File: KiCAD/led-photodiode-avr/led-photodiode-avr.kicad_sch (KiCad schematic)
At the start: 40 parts, among them J1 Screw_Terminal_01x02, J2 Conn_02x08_Odd_Even, J3 ISP, J4 Conn_01x06_Pin, U1 REF3040, U2 L78L05_SOT89, U3 OPA350, U4 L78L05_SOT89, U5 DDC112, U7 ATmega328-A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

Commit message: working on BOM
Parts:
- C1: value 0.47uF -> 0.33uF; DigikeyNumber (none) -> 1276-1123-1-ND; ManufacturerNumber (none) -> CL21B334KBFNNNE
- C10, C12, C14, C23, C3, C5, C54, C55, C6, C8: DigikeyNumber (none) -> 478-KGM21NR71H104KTCT-ND; ManufacturerNumber (none) -> KGM21NR71H104KT
- C11, C13, C4, C9: DigikeyNumber (none) -> 1292-0805X106K250CT-ND; ManufacturerNumber (none) -> 0805X106K250CT
- C19, C20: now not fitted
- C2, C7: DigikeyNumber (none) -> 1276-1123-1-ND; ManufacturerNumber (none) -> CL21B334KBFNNNE
- C52: DigikeyNumber (none) -> 1276-1029-1-ND; ManufacturerNumber (none) -> CL21B105KBFNNNE
- D3: DigikeyNumber (none) -> 1516-QBLP631-R3ACT-ND; ManufacturerNumber (none) -> QBLP631-R3A
- J1: DigikeyNumber (none) -> A98076-ND; ManufacturerNumber (none) -> 282836-2

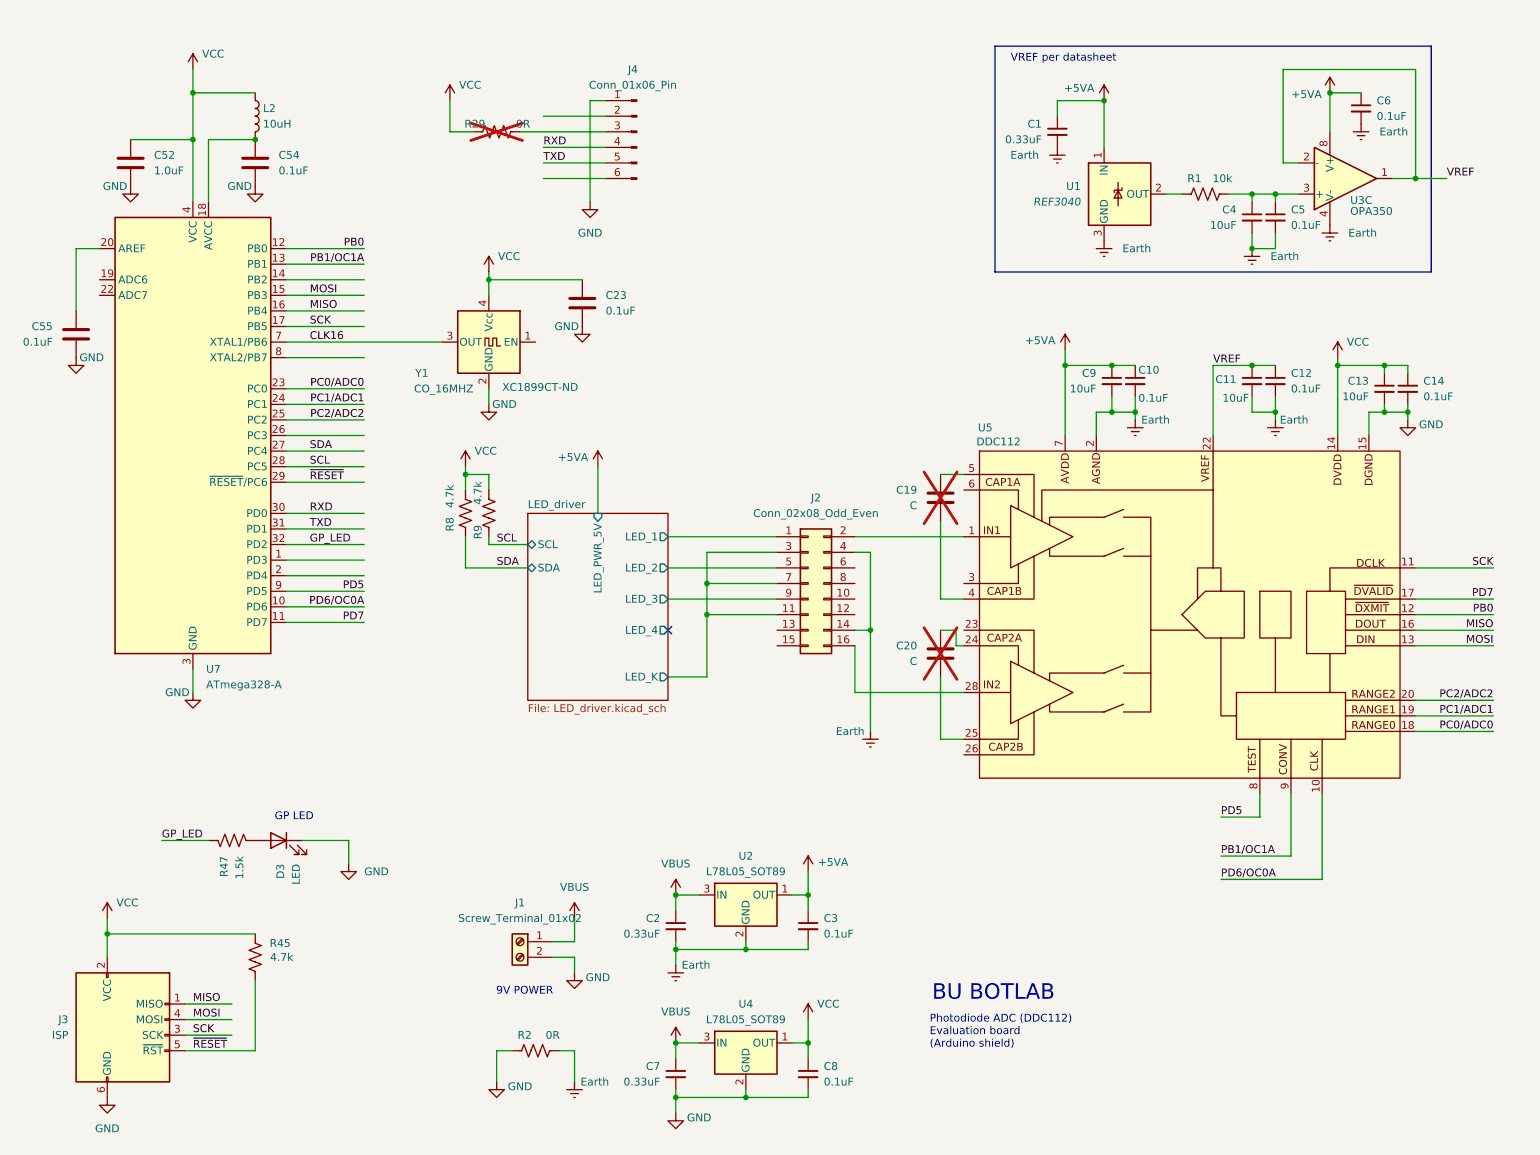
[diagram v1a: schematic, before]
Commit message: many schematic tweaks; add fields for BOM
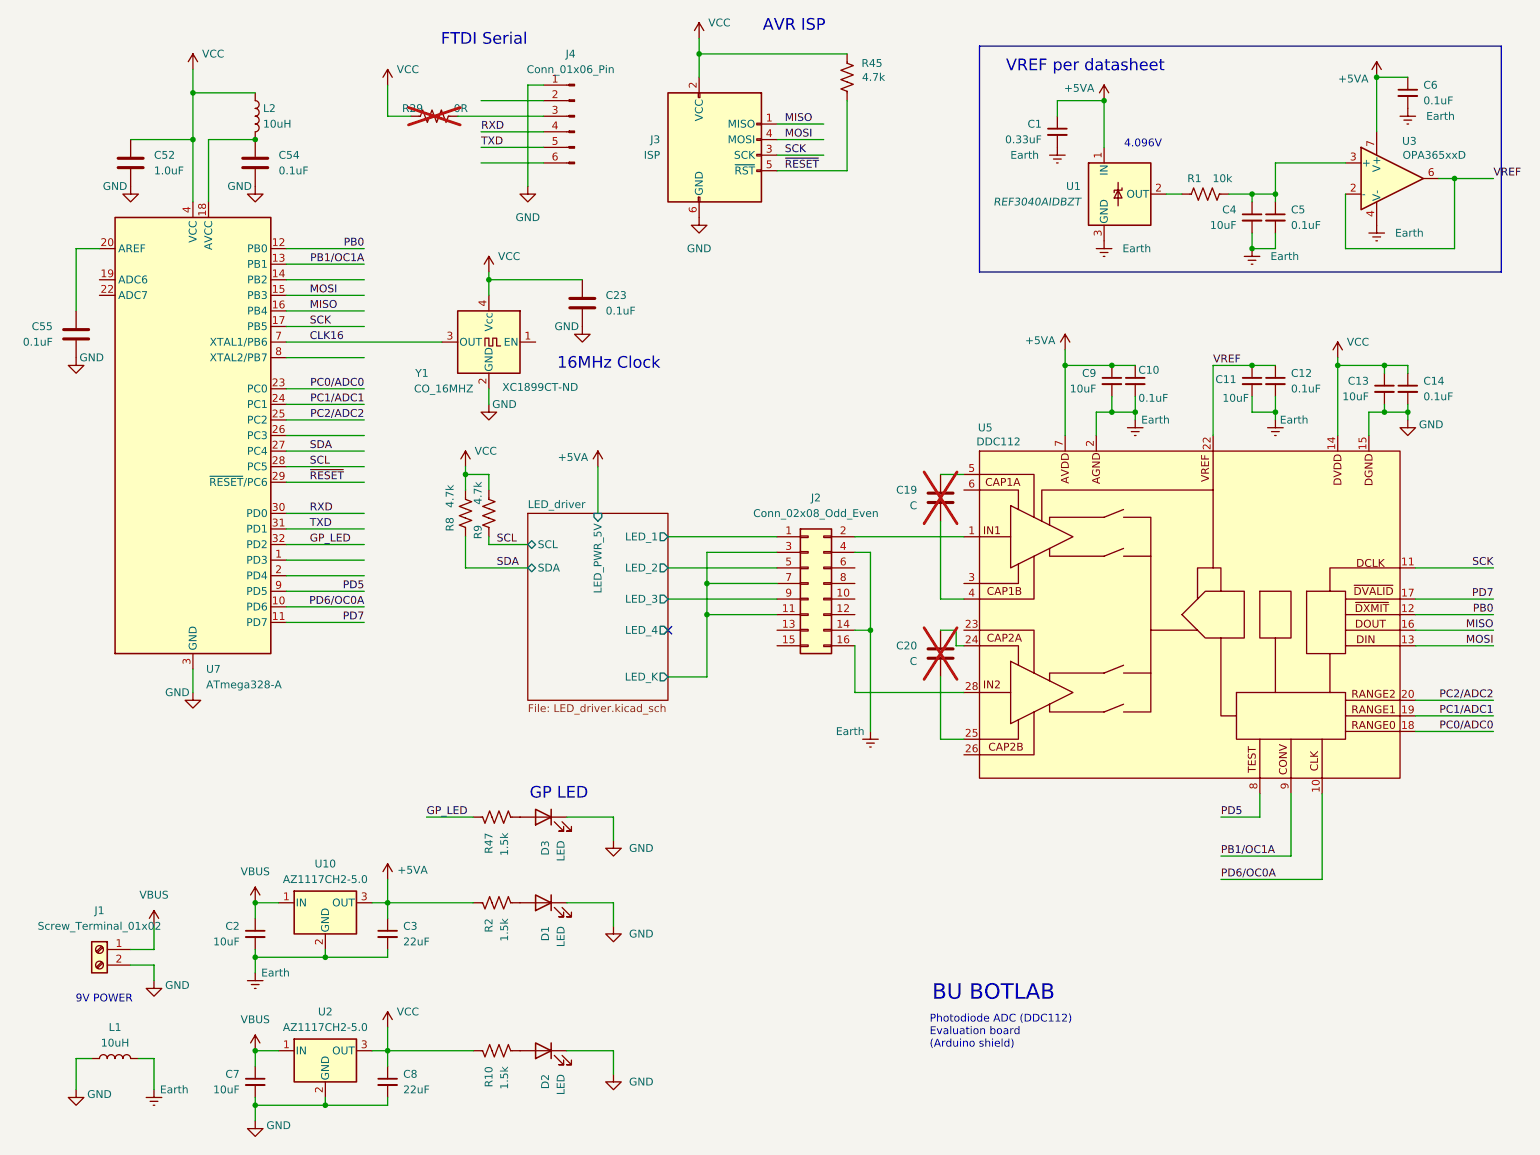
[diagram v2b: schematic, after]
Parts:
- removed U2, U4: L78L05_SOT89, Package_TO_SOT_SMD:SOT-89-3, symbol Regulator_Linear:L78L05_SOT89
- removed U3: OPA350, Package_SO:SOIC-8_3.9x4.9mm_P1.27mm, symbol Amplifier_Operational:LM358
- added D1, D2: LED, LED_SMD:LED_0805_2012Metric_Pad1.15x1.40mm_HandSolder, symbol Device:LED
- added L1: 10uH, Inductor_SMD:L_0805_2012Metric_Pad1.15x1.40mm_HandSolder, symbol Device:L
- added R10: 1.5k, Resistor_SMD:R_0805_2012Metric_Pad1.20x1.40mm_HandSolder, symbol Device:R_US
- added U10, U2: AZ1117CH2-5.0, Package_TO_SOT_SMD:SOT-223-3_TabPin2, symbol Regulator_Linear:AZ1117CH2-5.0
- added U3: OPA365xxD, Package_SO:SOIC-8_3.9x4.9mm_P1.27mm, symbol Amplifier_Operational:OPA365xxD
- C2, C7: value 0.33uF -> 10uF; DigikeyNumber 1276-1123-1-ND -> 1292-0805X106K250CT-ND; ManufacturerNumber CL21B334KBFNNNE -> 0805X106K250CT
- C3, C8: value 0.1uF -> 22uF; DigikeyNumber 478-KGM21NR71H104KTCT-ND -> 1276-CL21A226MAYNNNECT-ND; ManufacturerNumber KGM21NR71H104KT -> CL21A226MAYNNNE
- J2: DigikeyNumber (none) -> 10129381-916001BLF-ND; ManufacturerNumber (none) -> 10129381-916001BLF
- J3: DigikeyNumber (none) -> 1849-PR20203VBDN-ND; ManufacturerNumber (none) -> PR20203VBDN
- L2: footprint Inductor_SMD:L_0603_1608Metric_Pad1.05x0.95mm_HandSolder -> Inductor_SMD:L_0805_2012Metric_Pad1.15x1.40mm_HandSolder; DigikeyNumber (none) -> 445-6762-1-ND; ManufacturerNumber (none) -> MLZ2012N100LT000
- R1: DigikeyNumber (none) -> P10KACT-ND; ManufacturerNumber (none) -> ERJ-6GEYJ103V
- R2: value 0R -> 1.5k; CatNo (none) -> YAG1570CT-ND; DigikeyNumber (none) -> 541-4161-1-ND; ManufacturerNumber (none) -> CRCW08051K50FKEAC; MfgNo (none) -> RT0603BRD071K5L
- R45, R8, R9: DigikeyNumber (none) -> 541-4131-1-ND; ManufacturerNumber (none) -> CRCW08054K70FKEAC
- R47: DigikeyNumber (none) -> 541-4161-1-ND; ManufacturerNumber (none) -> CRCW08051K50FKEAC
- U1: value REF3040 -> REF3040AIDBZT; DigikeyNumber (none) -> REF3040AIDBZTCT-ND; ManufacturerNumber (none) -> REF3040AIDBZT
- U5: DigikeyNumber (none) -> 296-DDC112U/1KCT-ND; ManufacturerNumber (none) -> DDC112U/1K
- U7: DigikeyNumber (none) -> ATMEGA328P-AU-ND; ManufacturerNumber (none) -> ATMEGA328P-AU
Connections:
- net +5VA: now also R2.1, U10.3 (OUT), U3.7 (V+)
- net Earth: now also L1.2, U10.2 (GND), U3.4 (V-); no longer R2.2
- net GND: now also D1.1 (K), D2.1 (K), L1.1, U2.2 (GND); no longer R2.1
- net VBUS: now also U10.1 (IN), U2.1 (IN)
- net VCC: now also R10.1, U2.3 (OUT)
- net VREF: now also U3.2 (-), U3.6
- net at C4.1, C5.1, R1.2: now also U3.3 (+)
- new net: D2.2 (A), R10.2
- new net: D1.2 (A), R2.2
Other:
- note added: "16MHz Clock"
- note added: "4.096V"
- note added: "AVR ISP"
- note added: "FTDI Serial"
- moved on the sheet: C2, C3, C6, C7, C8, D3, J1, J3, J4, R29, R45, R47

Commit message: routing done
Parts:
- added H1, H2, H3, H4: MountingHole, MountingHole:MountingHole_4.3mm_M4_DIN965_Pad, symbol Mechanical:MountingHole
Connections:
- net Earth: now also D1.1 (K)
- net GND: no longer D1.1 (K)
- net LED_driver/LED_1: now also J2.9 (Pin_9); no longer J2.1 (Pin_1)
- net LED_driver/LED_3: now also J2.1 (Pin_1); no longer J2.9 (Pin_9)

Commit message: ready for review (update PDF, gerber)
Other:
- note added: "1.0"
- note added: "Photodiode ADC (DDC112) Evaluation board"
- note removed: "Photodiode ADC (DDC112) Evaluation board (Arduino shield)"
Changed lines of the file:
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@@
+		)
+	)
+	(text "1.0"
+		(exclude_from_sim no)
+		(at 254.254 199.39 0)
+		(effects
+			(font
+				(size 1.27 1.27)
+			)
 		)
 	)
@@
 		)
 	)
-	(text "Photodiode ADC (DDC112)\nEvaluation board\n(Arduino shield)"
+	(text "Photodiode ADC (DDC112)\nEvaluation board\n"
 		(exclude_from_sim no)
 		(at 163.322 182.372 0)

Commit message: small tweaks
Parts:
- J3: footprint Connector_PinHeader_2.54mm:PinHeader_2x03_P2.54mm_Vertical -> Connector_IDC:IDC-Header_2x03_P2.54mm_Horizontal; DigikeyNumber 1849-PR20203VBDN-ND -> 952-2092-ND; ManufacturerNumber PR20203VBDN -> M20-9950345
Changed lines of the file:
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@@
 			)
 		)
-		(property "Footprint" "Connector_PinHeader_2.54mm:PinHeader_2x03_P2.54mm_Vertical"
+		(property "Footprint" "Connector_IDC:IDC-Header_2x03_P2.54mm_Horizontal"
 			(at 121.92 38.1 90)
 			(effects
@@
 			)
 		)
-		(property "DigikeyNumber" "1849-PR20203VBDN-ND"
+		(property "DigikeyNumber" "952-2092-ND"
 			(at 128.27 39.37 0)
 			(effects
@@
 			)
 		)
-		(property "ManufacturerNumber" "PR20203VBDN"
+		(property "ManufacturerNumber" "M20-9950345"
 			(at 128.27 39.37 0)
 			(effects

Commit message: V1.0 as built
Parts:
- added D4: LED, LED_SMD:LED_0805_2012Metric_Pad1.15x1.40mm_HandSolder, symbol Device:LED
- added R11: 1.5k, Resistor_SMD:R_0805_2012Metric_Pad1.20x1.40mm_HandSolder, symbol Device:R_US
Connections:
- net GND: now also D4.1 (K)
- net GP_LED2: now reaches U7.1 (PD3)
- net GP_LED2: now also R11.1
- net SS/DONT_USE: now reaches U7.14 (PB2)
- new net: D4.2 (A), R11.2
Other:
- moved on the sheet: D3, R47

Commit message: more tests
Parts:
- added N1: Optical_PCB, optical_pcb_model:optical_pcb, symbol Mechanical:Housing
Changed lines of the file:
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@@
+	)
+	(symbol
+		(lib_id "Mechanical:Housing")
+		(at 177.8 157.48 0)
+		(unit 1)
+		(exclude_from_sim no)
+		(in_bom yes)
+		(on_board yes)
+		(dnp no)
+		(fields_autoplaced yes)
+		(property "Reference" "N1"
+			(at 181.61 156.5274 0)
+			(effects
+				(font
+					(size 1.27 1.27)
+				)
+				(justify left)
+			)
+		)
+		(property "Value" "Optical_PCB"
+			(at 181.61 159.0674 0)
+			(effects
+				(font
+					(size 1.27 1.27)
+				)
+				(justify left)
+			)
+		)
+		(property "Footprint" "optical_pcb_model:optical_pcb"
+			(at 179.07 156.21 0)
+			(effects
+				(font
+					(size 1.27 1.27)
+				)
+				(hide yes)
+			)
+		)
+		(property "Datasheet" "~"
+			(at 179.07 156.21 0)
+			(effects
+				(font
+					(size 1.27 1.27)
+				)
+				(hide yes)
+			)
+		)
+		(property "Description" "Housing"
+			(at 177.8 157.48 0)
+			(effects
+				(font
+					(size 1.27 1.27)
+				)
+				(hide yes)
+			)
+		)
+		(instances
+			(project ""
+				(path "/e63e39d7-6ac0-4ffd-8aa3-1841a4541b55"
+					(reference "N1")
+					(unit 1)
+				)
+			)
+		)
 	)
 	(symbol
